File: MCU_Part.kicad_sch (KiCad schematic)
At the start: 1 part, among them U1 STM32G473RCTx

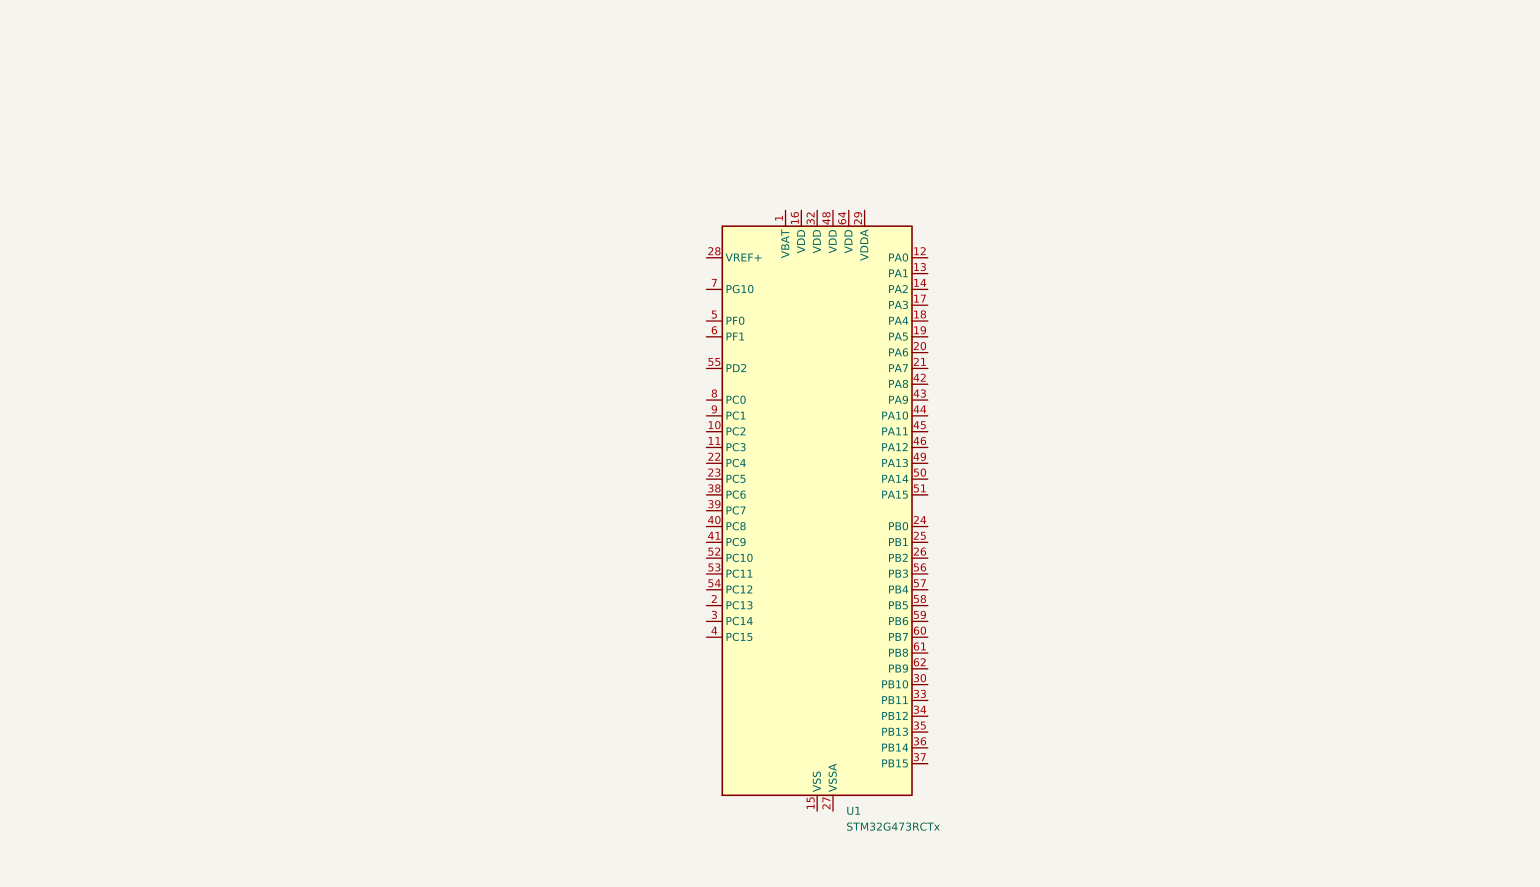
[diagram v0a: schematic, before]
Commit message: 增加PWM/SPI部分接口
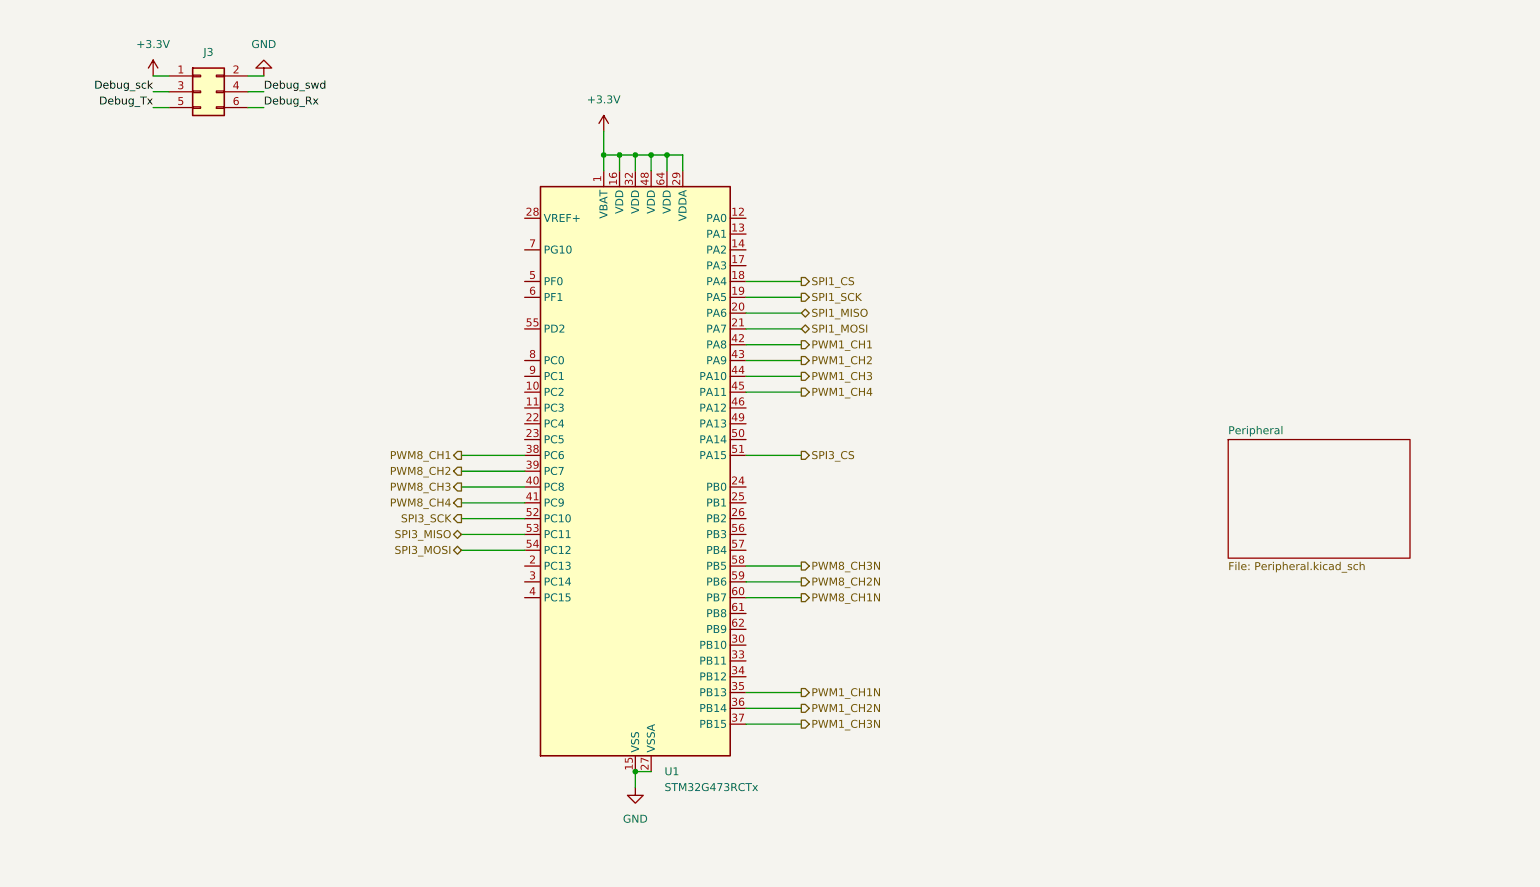
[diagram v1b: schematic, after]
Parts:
- added J3: Conn_02x03_Odd_Even, symbol Connector_Generic:Conn_02x03_Odd_Even
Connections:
- net +3.3V: now reaches U1.1 (VBAT)
- net +3.3V: now also U1.16 (VDD), U1.29 (VDDA), U1.32 (VDD), U1.48 (VDD), U1.64 (VDD), J3.1 (Pin_1)
- net GND: now reaches U1.15 (VSS), U1.31 (VSS), U1.47 (VSS), U1.63 (VSS)
- net GND: now also U1.27 (VSSA), J3.2 (Pin_2)
- net SPI1_CS: now reaches U1.18 (PA4)
- net SPI1_SCK: now reaches U1.19 (PA5)
- net SPI1_MISO: now reaches U1.20 (PA6)
- net SPI1_MOSI: now reaches U1.21 (PA7)
- net PWM1_CH1N: now reaches U1.35 (PB13)
- net PWM1_CH2N: now reaches U1.36 (PB14)
- net PWM1_CH3N: now reaches U1.37 (PB15)
- net PWM8_CH1: now reaches U1.38 (PC6)
- net PWM8_CH2: now reaches U1.39 (PC7)
- net PWM8_CH3: now reaches U1.40 (PC8)
- net PWM8_CH4: now reaches U1.41 (PC9)
- net PWM1_CH1: now reaches U1.42 (PA8)
- net PWM1_CH2: now reaches U1.43 (PA9)
- net PWM1_CH3: now reaches U1.44 (PA10)
- net PWM1_CH4: now reaches U1.45 (PA11)
- net SPI3_CS: now reaches U1.51 (PA15)
- net SPI3_SCK: now reaches U1.52 (PC10)
- net SPI3_MISO: now reaches U1.53 (PC11)
- net SPI3_MOSI: now reaches U1.54 (PC12)
- net PWM8_CH3N: now reaches U1.58 (PB5)
- net PWM8_CH2N: now reaches U1.59 (PB6)
- net PWM8_CH1N: now reaches U1.60 (PB7)
- new net Debug_Rx: J3.6 (Pin_6)
- new net Debug_Tx: J3.5 (Pin_5)
- new net Debug_sck: J3.3 (Pin_3)
- new net Debug_swd: J3.4 (Pin_4)
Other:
- added sheet Peripheral (Peripheral.kicad_sch)
- moved on the sheet: U1

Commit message: 增加ADC采样，优化PWM
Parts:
- added U4: TJA1051T, Package_SO:SOIC-8_3.9x4.9mm_P1.27mm, symbol Interface_CAN_LIN:TJA1051T
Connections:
- net PC1_ADC1_IN8: now reaches U1.10 (PC2)
- net PC1_ADC2_IN9: now reaches U1.11 (PC3)
- net PA0_ADC2_IN1: now reaches U1.12 (PA0)
- net PA1_ADC2_IN2: now reaches U1.13 (PA1)
- net PB10_TIM1_BREAK: now reaches U1.30 (PB10)
- net PB12_ADC1_IN11: now reaches U1.33 (PB11)
- net PB11_ADC2_IN14: now reaches U1.34 (PB12)
- net PD2_TIM8_BREAK: now reaches U1.55 (PD2)
- net PC0_ADC1_IN6: now reaches U1.8 (PC0)
- net PC1_ADC1_IN7: now reaches U1.9 (PC1)

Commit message: 完成部分I2C/FDCAN引脚分配
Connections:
- net Debug_Rx: now also U1.22 (PC4)
- net Debug_Tx: now also U1.23 (PC5)
- net Debug_sck: now also U1.50 (PA14)
- net Debug_swd: now also U1.49 (PA13)
- net PWM8_CH1N: now also U1.56 (PB3); no longer U1.60 (PB7)
- net PWM8_CH2N: now also U1.57 (PB4); no longer U1.59 (PB6)
- net PB0_ADC1_IN15: now reaches U1.24 (PB0)
- net Peripheral/24C02_SCL: now reaches U1.61 (PB8)
- net PB12_ADC1_IN11 renamed PB12_FDCAN2_RX
- new net PB6_FDCAN2_TX: U1.59 (PB6)
- new net Peripheral/24C02_SCA: U1.60 (PB7)
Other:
- sheet Peripheral ports: added 24C02_SCA, 24C02_SCL; removed none
- moved on the sheet: U4
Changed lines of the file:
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@@
+	(wire
+		(pts
+			(xy 83.82 85.09) (xy 93.98 85.09)
+		)
+		(stroke
+			(width 0)
+			(type default)
+		)
+	)
 	(wire
 		(pts
@@
 	(wire
 		(pts
-			(xy 129.54 113.03) (xy 138.43 113.03)
+			(xy 129.54 113.03) (xy 186.69 113.03)
+		)
+		(stroke
+			(width 0)
+			(type default)
+		)
+	)
+	(wire
+		(pts
+			(xy 129.54 105.41) (xy 138.43 105.41)
 		)
 		(stroke
@@
 	(wire
 		(pts
+			(xy 129.54 115.57) (xy 186.69 115.57)
+		)
+		(stroke
+			(width 0)
+			(type default)
+		)
+	)
+	(wire
+		(pts
 			(xy 34.29 31.75) (xy 36.83 31.75)
 		)
@@
 	(wire
 		(pts
+			(xy 129.54 102.87) (xy 138.43 102.87)
+		)
+		(stroke
+			(width 0)
+			(type default)
+		)
+	)
+	(wire
+		(pts
 			(xy 129.54 77.47) (xy 138.43 77.47)
 		)
@@
 	(wire
 		(pts
+			(xy 129.54 87.63) (xy 138.43 87.63)
+		)
+		(stroke
+			(width 0)
+			(type default)
+		)
+	)
+	(wire
+		(pts
 			(xy 129.54 133.35) (xy 138.43 133.35)
 		)
@@
 	(wire
 		(pts
+			(xy 83.82 87.63) (xy 93.98 87.63)
+		)
+		(stroke
+			(width 0)
+			(type default)
+		)
+	)
+	(wire
+		(pts
 			(xy 129.54 90.17) (xy 138.43 90.17)
 		)
@@
 	(wire
 		(pts
+			(xy 129.54 85.09) (xy 138.43 85.09)
+		)
+		(stroke
+			(width 0)
+			(type default)
+		)
+	)
+	(wire
+		(pts
 			(xy 119.38 41.91) (xy 119.38 44.45)
 		)
@@
 		(pts
 			(xy 49.53 34.29) (xy 52.07 34.29)
+		)
+		(stroke
+			(width 0)
+			(type default)
+		)
+	)
+	(wire
+		(pts
+			(xy 129.54 95.25) (xy 138.43 95.25)
 		)
 		(stroke
@@
 	)
 	(label "Debug_sck"
+		(at 138.43 87.63 0)
+		(effects
+			(font
+				(size 1.27 1.27)
+			)
+			(justify left bottom)
+		)
+	)
+	(label "Debug_sck"
 		(at 34.29 31.75 180)
+		(effects
+			(font
+				(size 1.27 1.27)
+			)
+			(justify right bottom)
+		)
+	)
+	(label "Debug_Tx"
+		(at 83.82 87.63 180)
+		(effects
+			(font
+				(size 1.27 1.27)
+			)
+			(justify right bottom)
+		)
+	)
+	(label "Debug_swd"
+		(at 138.43 85.09 0)
+		(effects
+			(font
+				(size 1.27 1.27)
+			)
+			(justify left bottom)
+		)
+	)
+	(label "Debug_Rx"
+		(at 83.82 85.09 180)
 		(effects
 			(font
@@
 	(hierarchical_label "PWM8_CH2N"
 		(shape output)
-		(at 138.43 110.49 0)
+		(at 138.43 105.41 0)
 		(effects
 			(font
@@
 		)
 	)
-	(hierarchical_label "PB12_ADC1_IN11"
-		(shape input)
+	(hierarchical_label "PB12_FDCAN2_RX"
+		(shape bidirectional)
 		(at 138.43 123.19 0)
 		(effects
@@
 		)
 	)
+	(hierarchical_label "PB6_FDCAN2_TX"
+		(shape bidirectional)
+		(at 138.43 110.49 0)
+		(effects
+			(font
+				(size 1.27 1.27)
+			)
+			(justify left)
+		)
+	)
 	(hierarchical_label "PWM1_CH3"
 		(shape output)
 		(at 138.43 77.47 0)
+		(effects
+			(font
+				(size 1.27 1.27)
+			)
+			(justify left)
+		)
+	)
+	(hierarchical_label "PB0_ADC1_IN15"
+		(shape input)
+		(at 138.43 95.25 0)
 		(effects
 			(font
@@
 	(hierarchical_label "PWM8_CH1N"
 		(shape output)
-		(at 138.43 113.03 0)
+		(at 138.43 102.87 0)
 		(effects
 			(font
@@
 	(symbol
 		(lib_id "Interface_CAN_LIN:TJA1051T")
-		(at 217.17 128.27 0)
+		(at 201.93 147.32 0)
 		(unit 1)
 		(exclude_from_sim no)
@@
 		(fields_autoplaced yes)
 		(property "Reference" "U4"
-			(at 219.3133 115.57 0)
+			(at 204.0733 134.62 0)
 			(effects
 				(font
@@
 		)
 		(property "Value" "TJA1051T"
-			(at 219.3133 118.11 0)
+			(at 204.0733 137.16 0)
 			(effects
 				(font
@@
 		)
 		(property "Footprint" "Package_SO:SOIC-8_3.9x4.9mm_P1.27mm"
-			(at 217.17 140.97 0)
+			(at 201.93 160.02 0)
 			(effects
 				(font
@@
 		)
 		(property "Datasheet" "http://www.nxp.com/docs/en/data-sheet/TJA1051.pdf"
-			(at 217.17 128.27 0)
+			(at 201.93 147.32 0)
 			(effects
 				(font
@@
 		)
 		(property "Description" "High-Speed CAN Transceiver, silent mode, SOIC-8"
-			(at 217.17 128.27 0)
+			(at 201.93 147.32 0)
 			(effects
 				(font
@@
 	)
 	(sheet
-		(at 207.01 87.63)
+		(at 186.69 110.49)
 		(size 29.21 19.05)
 		(exclude_from_sim no)
@@
 		)
 		(fill
-			(color 0 0 0 0.0000)
+			(color 194 194 0 1.0000)
 		)
 		(property "Sheetname" "Peripheral"
-			(at 207.01 86.9184 0)
+			(at 186.69 109.7784 0)
 			(effects
 				(font
@@
 		)
 		(property "Sheetfile" "Peripheral.kicad_sch"
-			(at 207.01 107.2646 0)
+			(at 186.69 130.1246 0)
 			(effects
 				(font
@@
 			)
 		)
+		(pin "24C02_SCL" input
+			(at 186.69 115.57 180)
+			(effects
+				(font
+					(size 1.27 1.27)
+				)
+				(justify left)
+			)
+		)
+		(pin "24C02_SCA" input
+			(at 186.69 113.03 180)
+			(effects
+				(font
+					(size 1.27 1.27)
+				)
+				(justify left)
+			)
+		)

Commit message: 增加3.3V电路
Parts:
- added R1, R2: 10K, symbol Device:R_Small_US
- added R4: 120R, symbol Device:R_Small_US
- added R5: 0R, symbol Device:R_Small_US
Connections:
- net PB12_FDCAN2_RX is gone; now on an unnamed net: U1.33 (PB11)
- net PB6_FDCAN2_TX is gone; now on an unnamed net: U1.59 (PB6)
- net +3.3V: now also U1.28 (VREF+), R1.1, R2.1, R5.1; no longer J3.1 (Pin_1)
- net Peripheral/24C02_SCL: now also R1.2
- net CAN_L: now reaches U4.6 (CANL)
- net CAN_L: now also R4.2
- net CAN_H: now reaches U4.7 (CANH)
- net CAN_H: now also R4.1
- net Peripheral/24C02_SCA renamed Peripheral/24C02_SDA
- net Peripheral/24C02_SDA: now also R2.2
- new net: J3.1 (Pin_1), R5.2
- no-connect marks 0 -> 15
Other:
- sheet Peripheral ports: added 24C02_SDA, ICM-20602-SCL, ICM-20602-SDA; removed 24C02_SCA
- moved on the sheet: J3, U4

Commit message: 优化EEPROM电路
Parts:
- removed J3: Conn_02x03_Odd_Even, symbol Connector_Generic:Conn_02x03_Odd_Even
- removed R5: 0R, symbol Device:R_Small_US
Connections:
- net Debug_Rx renamed PC4_UART1_RX
- net Debug_Tx renamed PC5_UART1_TX
- net Debug_sck renamed PA14_SWD_SCK
- net Debug_swd renamed PA13_SWD_SDO

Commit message: 优化IMU电路
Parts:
- added C4, C5, C6: 18pF, symbol Device:C_Small
- added R7: R_Small_US, symbol Device:R_Small_US
- added SW1: SW_Push, symbol Switch:SW_Push
- added Y1: 12MHZ, symbol Device:Crystal_GND24_Small
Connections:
- net +3.3V: now also R7.1
- net GND: now also C4.2, C5.1, C6.2, SW1.2, Y1.2, Y1.4
- net at U1.5 (PF0): now also C4.1, Y1.3
- net at U1.6 (PF1): now also C5.2, Y1.1
- net at U1.7 (PG10): now also C6.1, R7.2, SW1.1
- no-connect marks 15 -> 12

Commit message: 优化IMU电路
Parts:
- removed C4, C5, C6: 18pF, symbol Device:C_Small
- removed R7: R_Small_US, symbol Device:R_Small_US
- removed SW1: SW_Push, symbol Switch:SW_Push
- removed Y1: 12MHZ, symbol Device:Crystal_GND24_Small
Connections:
- net Peripheral/ICM-20602-INT: now reaches U1.62 (PB9)
- no-connect marks 12 -> 14
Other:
- sheet Peripheral ports: added ICM-20602-INT; removed none
- moved on the sheet: R1, R2

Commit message: 优化接口
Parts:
- removed R4: 120R, symbol Device:R_Small_US
- removed U4: TJA1051T, Package_SO:SOIC-8_3.9x4.9mm_P1.27mm, symbol Interface_CAN_LIN:TJA1051T
- added C11, C12, C13, C14, C15, C16, C17: 0.1uF, Capacitor_SMD:C_0603_1608Metric_Pad1.08x0.95mm_HandSolder, symbol Device:C_Small
- R1, R2: footprint (none) -> Resistor_SMD:R_0603_1608Metric_Pad0.98x0.95mm_HandSolder
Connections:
- net +3.3V: now also C11.1, C12.1, C13.1, C14.1, C15.1, C16.1, C17.1
- net GND: now also C11.2, C12.2, C13.2, C14.2, C15.2, C16.2, C17.2
- net Peripheral/PB6_FDCAN2_TX: now reaches U1.59 (PB6)
- net Peripheral/PB11_FDCAN2_RX: now reaches U1.33 (PB11)
- net PWM1_CH1 renamed PA8_TIM1_CH1
- net PWM1_CH1N renamed PB13_TIM1_CH1N
- net PWM1_CH2 renamed PA9_TIM1_CH2
- net PWM1_CH2N renamed PB14_TIM1_CH2N
- net PWM1_CH3 renamed PA10_TIM1_CH3
- net PWM1_CH3N renamed PB15_TIM1_CH3N
- net PWM1_CH4 renamed PA11_TIM1_CH4
- net PWM8_CH1 renamed PC6_TIM8_CH1
- net PWM8_CH1N renamed PB3_TIM8_CH1N
- net PWM8_CH2 renamed PC7_TIM8_CH2
- net PWM8_CH2N renamed PB4_TIM8_CH2N
- net PWM8_CH3 renamed PC8_TIM8_CH3
- net PWM8_CH3N renamed PB5_TIM8_CH3N
- net PWM8_CH4 renamed PC9_TIM8_CH4
- net SPI1_CS renamed PA4_SPI1_CS
- net SPI1_MISO renamed PA6_SPI1_MISO
- net SPI1_MOSI renamed PA7_SPI1_MOSI
- net SPI1_SCK renamed PA5_SPI1_SCK
- net SPI3_CS renamed PA15_SPI3_CS
- net SPI3_MISO renamed PC11_SPI3_MISO
- net SPI3_MOSI renamed PC12_SPI3_MOSI
- net SPI3_SCK renamed PC10_SPI3_SCK
- no-connect marks 14 -> 11
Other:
- sheet Peripheral ports: added PB11_FDCAN2_RX, PB6_FDCAN2_TX, TLE9251VSJ_H, TLE9251VSJ_L; removed none
